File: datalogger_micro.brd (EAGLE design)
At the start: 33 x 38.1 mm, 41 parts, among them IC1 DS3231/SO, IC3 LD117AS33TR, M0 PAT, M1 PAT

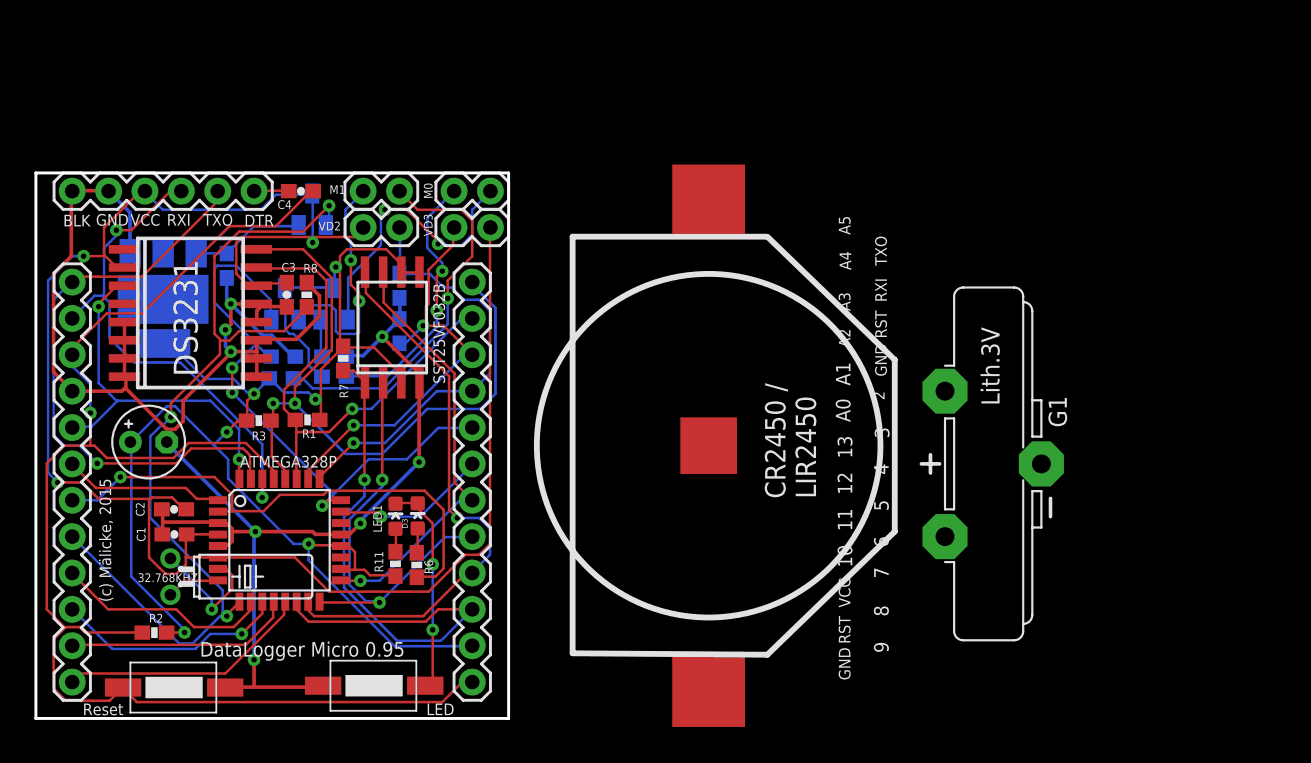
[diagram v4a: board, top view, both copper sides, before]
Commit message: one-sided
moved layout to one sided again, use SMT battery pack.
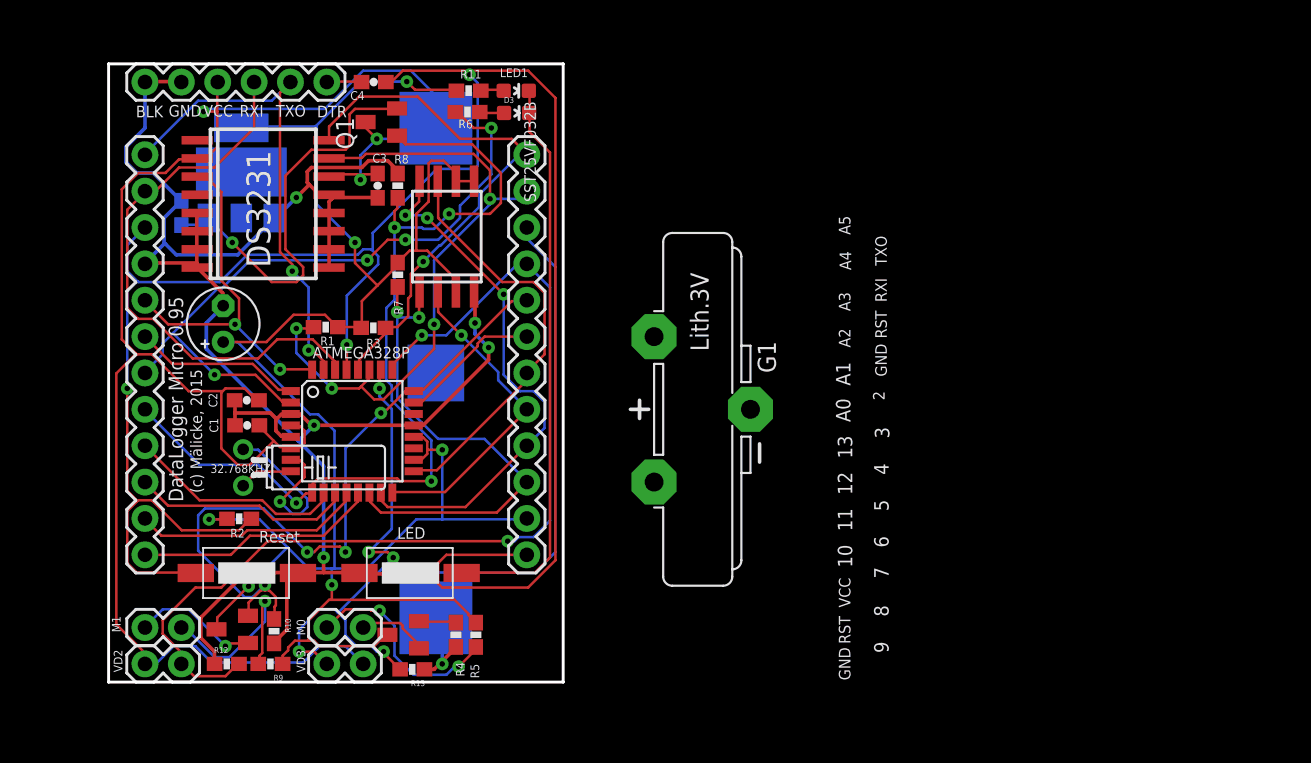
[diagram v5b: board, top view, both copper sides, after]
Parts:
- moved M1 34.1 mm to (7.62, 6.35)
- moved VD2 34.1 mm to (7.62, 3.81)
- moved R11 33.4 mm to (30.2, 43.8), turned to 180 degrees
- moved R6 31.8 mm to (30.1, 42.4), turned to 0 degrees
- moved VD3 31.8 mm to (22.9, 3.81)
- moved M0 31.8 mm to (22.9, 6.35)
- moved LED1 30.9 mm to (33.6, 43.8), turned to 270 degrees
- moved R12 29.0 mm to (13.3, 3.81), flipped to the top, turned to 0 degrees
- moved D3 29.0 mm to (33.6, 42.3), turned to 270 degrees
- moved R13 23.6 mm to (26.3, 3.43), flipped to the top, turned to 180 degrees
- moved Q2 23.6 mm to (25.7, 5.84), flipped to the top, turned to 90 degrees
- moved Q3 23.0 mm to (13.7, 6.22), flipped to the top, turned to 90 degrees
- moved R5 21.2 mm to (29.3, 5.84), flipped to the top, turned to 270 degrees
- moved G1 20.7 mm to (45.7, 21.6)
- moved R4 20.6 mm to (30.7, 5.84), flipped to the top, turned to 270 degrees
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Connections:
- net GND: no longer G1.-
- net VCC/2: no longer G1.+
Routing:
- net RESET: track 100.4 -> 145.8 mm, vias 1 -> 3
- net A3: track 29.6 -> 70.9 mm, vias 2 -> 5
- net A2: track 30.1 -> 69.6 mm, vias 1 -> 2
- net VCC-ST: track 114.1 -> 151.4 mm
- net GNDA: track 15.0 -> 39.9 mm, vias 2 -> 0
- net N$1: track 7.99 -> 29.3 mm, vias 0 -> 1
- net N$6: track 19.8 -> 5.05 mm, vias 2 -> 0
- net N$8: track 26.8 -> 13.8 mm
- net A5: track 48.9 -> 38.1 mm, vias 2 -> 1
- net D4: track 36.6 -> 47.4 mm, vias 1 -> 4
- net GND: track 139.9 -> 149.6 mm, vias 8 -> 7
- net A4: track 36.3 -> 45.7 mm, vias 1 -> 4
- net N$5: track 17.2 -> 8.90 mm, vias 2 -> 1
- net A1: track 42.6 -> 50.5 mm, vias 3 -> 4
- net MISO: track 30.4 -> 22.6 mm, vias 2 -> 1
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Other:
- board size 33 x 38.1 mm -> 31.8 x 43.2 mm

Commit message: schematic adaptions
a lot of schematic adaptions. included various C and Rs were neceassary.
MOSFET instead of Transistor on LM1117..
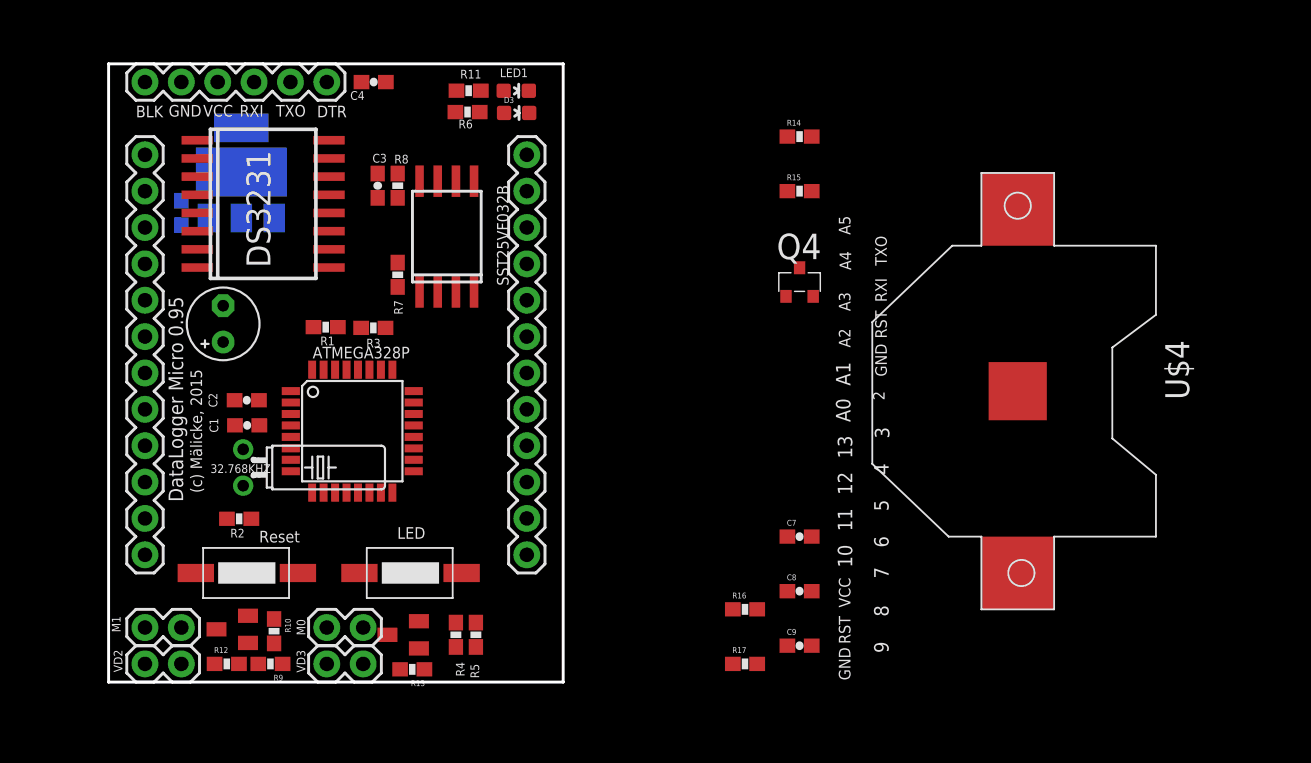
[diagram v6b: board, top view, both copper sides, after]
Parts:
- removed G1: CR2450V, battery:CR2450V
- removed Q1: (no value), semicon-smd-ipc:SOT23
- removed U$3: CR2450SMT, battery:CR2450SMT
- added C7, C8, C9: 0.1uF, SparkFun:0603-CAP
- added Q4: IRLML5203, transistor-power:MICRO3
- added R14, R15, R16, R17: VAR, SparkFun:0603-RES
- added U$4: LIR2032, adafruit:CR2032-SMD
- R8: value 10k -> 100k
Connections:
- net A2: now also R14.1
- net A3: now also R15.1
- net A6: now also ATMEGA328P.19, R16.2, R17.2; no longer IC1.4
- net D2: no longer IC1.3
- net D5: now also Q4.1; no longer Q1.1
- net GND: now also C7.1, C8.1, C9.1, Q4.2, R17.1, U$4.-; no longer IC3.1, U$3.P$2
- net N$1: now also IC3.1, Q4.3; no longer C6.1, IC3.3, Q1.2
- net VCC-ST: now also C9.2; no longer ATMEGA328P.18, R1.2, R3.2
- net VCC/2: now also ATMEGA328P.18, C6.1, C7.2, C8.2, IC3.3, R1.2, R14.2, R15.2, R16.1, R3.2, U$4.+$1, U$4.+$2; no longer Q1.3, U$3.P$3
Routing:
- net VCC-ST: track 151.4 -> 0.00 mm, vias 6 -> 0
- net GND: track 149.6 -> 0.00 mm, vias 7 -> 0
- net RESET: track 145.8 -> 0.00 mm, vias 3 -> 0
- net VCC/2: track 124.2 -> 0.00 mm, vias 3 -> 0
- net A3: track 70.9 -> 0.00 mm, vias 5 -> 0
- net A2: track 69.6 -> 0.00 mm, vias 2 -> 0
- net D5: track 63.9 -> 0.00 mm, vias 4 -> 0
- net A1: track 50.5 -> 0.00 mm, vias 4 -> 0
- net D4: track 47.4 -> 0.00 mm, vias 4 -> 0
- net A4: track 45.7 -> 0.00 mm, vias 4 -> 0
- net GNDA: track 39.9 -> 0.00 mm
- net RXI: track 39.1 -> 0.00 mm
- net A5: track 38.1 -> 0.00 mm, vias 1 -> 0
- net MOSI: track 37.4 -> 0.00 mm, vias 3 -> 0
- net D10: track 35.4 -> 0.00 mm, vias 2 -> 0
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
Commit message: schematics finalized
schematics are finalized and will be verified
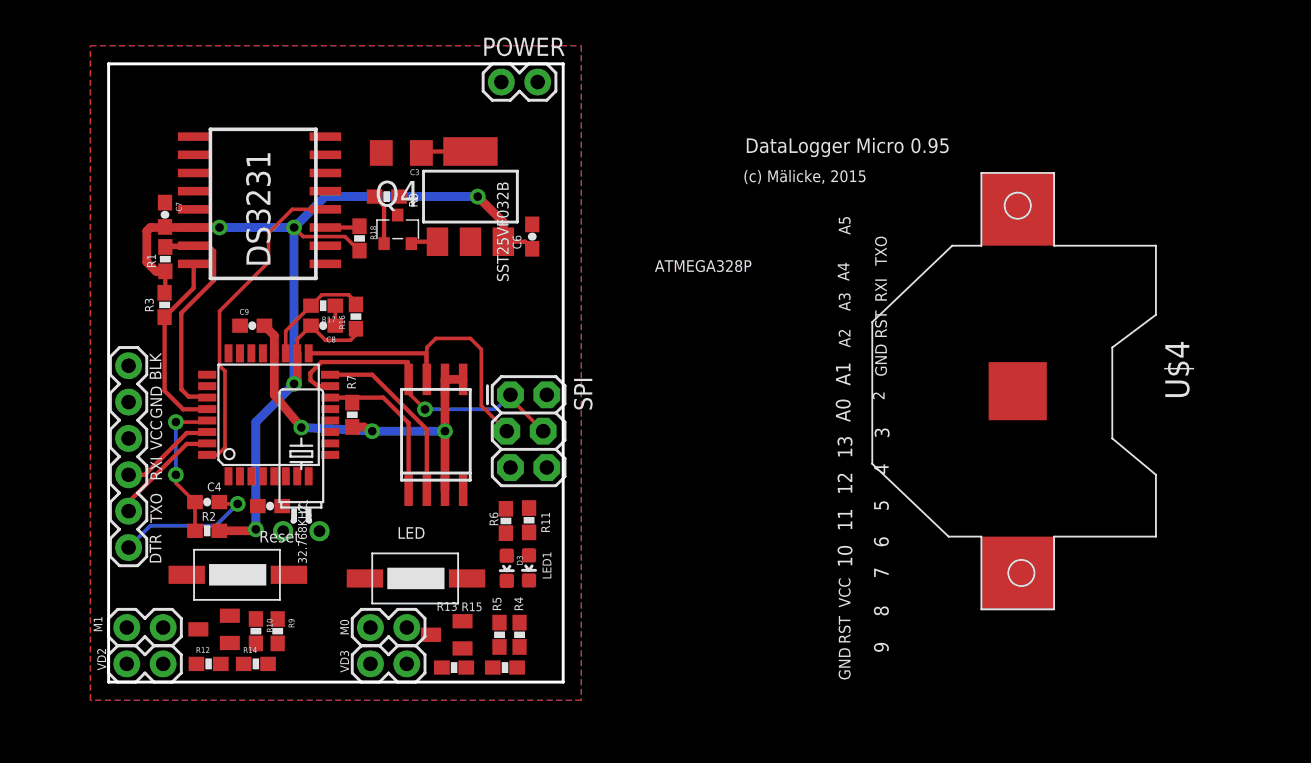
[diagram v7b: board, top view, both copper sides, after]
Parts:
- removed C2: 0.1uF, SparkFun:0603-CAP
- removed C5: 10uF, rcl:E2,5-5
- removed JP3, JP7: (no value), SparkFun:1X12
- added POWER: (no value), SparkFun:1X02
- added R18: 10k, SparkFun:0603-RES
- added SPI: SPI, SparkFun-Connectors:2X3_LOCK
- C3: value 0.1uF -> 10uF; device SparkFun:0603-CAP -> SparkFun:1206
- moved R14 52.9 mm to (15.4, 3.81)
- moved C7 49.7 mm to (9.02, 35.2), turned to 270 degrees
- moved C9 44.3 mm to (15.1, 27.4)
- moved R15 39.1 mm to (32.8, 3.56)
- moved R17 38.7 mm to (20.1, 28.8), turned to 180 degrees
- moved C8 38.1 mm to (20.1, 27.4), turned to 180 degrees
- moved JP1 35.3 mm to (6.48, 11.9), turned to 90 degrees
- moved R16 34.0 mm to (22.4, 28.1), turned to 90 degrees
- moved LED1 33.3 mm to (34.4, 10.5), turned to 180 degrees
- moved D3 31.8 mm to (32.9, 10.5), turned to 180 degrees
- moved C4 31.6 mm to (12.0, 15.1), turned to 0 degrees
- moved R11 30.3 mm to (34.4, 13.8), turned to 90 degrees
- moved R6 28.7 mm to (32.8, 13.8), turned to 270 degrees
- moved Q4 28.3 mm to (25.3, 34.2)
- moved C6 24.6 mm to (34.7, 33.7), flipped to the top
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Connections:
- removed net VCC/2: ATMEGA328P.18, ATMEGA328P.4, ATMEGA328P.6, C1.2, C2.1, C3.2, C6.1, C7.2, C8.2, IC1.14, IC1.2, IC3.3, JP1.4, R1.2, R14.2, R15.2, R16.1, R3.2, U$4.+$1, U$4.+$2, VD2.1, VD3.1
- new net VBAT: ATMEGA328P.18, ATMEGA328P.4, ATMEGA328P.6, C1.2, C6.1, C7.2, C8.2, IC1.14, IC3.3, POWER.2, R1.2, R14.2, R15.2, R16.1, R18.2, R2.2, R3.2, U$4.+$1, U$4.+$2, VD2.1, VD3.1
- net A0: no longer JP3.7
- net A1: no longer JP3.8
- net A2: no longer JP3.9
- net A3: no longer JP3.10
- net A4: no longer JP3.11
- net A5: no longer JP3.12
- net D10: no longer JP3.3
- net D2: now also IC1.4; no longer JP7.8
- net D3: no longer JP7.7
- net D4: no longer JP7.6
- net D5: no longer JP7.5
- net D6: no longer JP7.4
- net D7: now also IC1.2; no longer JP7.3
- net D8: now also IC1.3, R18.1; no longer JP7.2
- net D9: no longer JP7.1
- net GND: now also C3.2, POWER.1, Q4.3, SPI.6; no longer C2.2, C3.1, C5.-, JP7.9, Q4.2
- net MISO: no longer JP3.5
- net MOSI: now also SPI.1, SPI.4; no longer JP3.4
- net N$1: now also Q4.2; no longer Q4.3
- net RESET: now also SPI.5; no longer JP3.1, JP7.10
- net RXI: no longer JP7.11
- net SCK: now also SPI.3; no longer JP3.6
- net TXO: no longer JP7.12
- net VCC-ST: now also C3.1; no longer C5.+, JP3.2, R2.2
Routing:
- net VBAT: track 0.00 -> 74.2 mm, vias 0 -> 5
- net VCC-ST: track 0.00 -> 32.1 mm, vias 0 -> 3
- net SCK: track 0.00 -> 23.1 mm
- net MOSI: track 0.00 -> 22.8 mm, vias 0 -> 1
- net D2: track 0.00 -> 22.7 mm
- net A4: track 0.00 -> 18.2 mm
- net A5: track 0.00 -> 13.2 mm
- net MISO: track 0.00 -> 12.6 mm
- net D10: track 0.00 -> 10.6 mm
- net RESET: track 0.00 -> 10.4 mm, vias 0 -> 2
- net DTR: track 0.00 -> 10.2 mm, vias 0 -> 1
- net A6: track 0.00 -> 7.88 mm
- net TXO: track 0.00 -> 7.82 mm
- net RXI: track 0.00 -> 6.73 mm
- net D5: track 0.00 -> 3.56 mm
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- added copper zone on layer 1, net GND
- added copper zone on layer 16, net GND

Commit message: routing
Routing is 90% complete
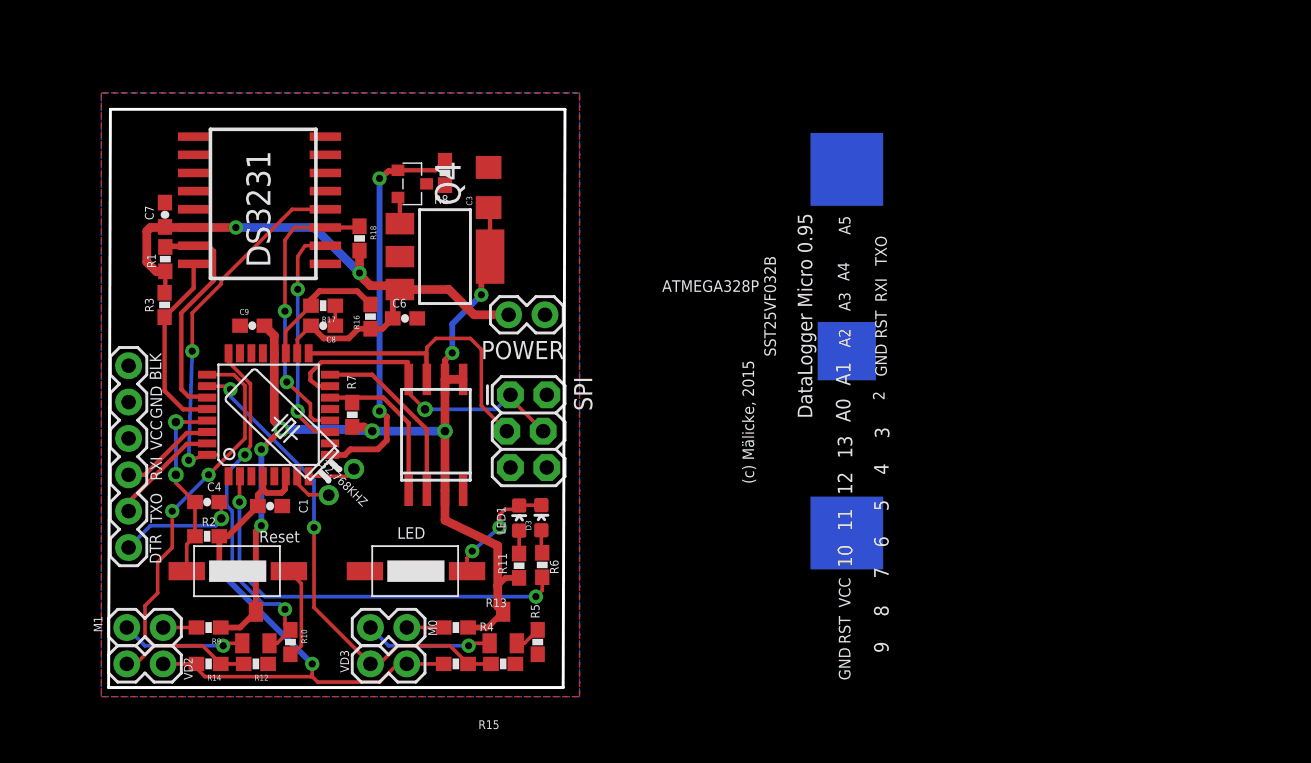
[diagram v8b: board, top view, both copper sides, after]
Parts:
- moved POWER 16.5 mm to (35.6, 28.2), turned to 180 degrees
- moved U$4 12.3 mm to (56.6, 25.7), flipped to the bottom
- moved C6 10.6 mm to (25.8, 27.9), turned to 0 degrees
- moved C3 6.56 mm to (31.6, 37.1), turned to 90 degrees
- moved R9 4.83 mm to (12.1, 6.35), turned to 180 degrees
- moved IC3 4.55 mm to (28.6, 32.3), turned to 270 degrees
- moved R4 4.47 mm to (29.3, 6.35), turned to 180 degrees
- moved 32.768KHZ 4.42 mm to (21.3, 16.5), turned to 46 degrees
- moved R8 4.39 mm to (28.6, 38.1), turned to 270 degrees
- moved D3 4.28 mm to (35.3, 14.0), turned to 0 degrees
- moved R6 3.98 mm to (35.4, 10.7), turned to 90 degrees
- moved Q2 3.97 mm to (32.6, 6.35), turned to 0 degrees
- moved LED1 3.55 mm to (33.8, 14.0), turned to 0 degrees
- moved R13 3.44 mm to (32.6, 3.81)
- moved R15 3.44 mm to (29.3, 3.81), turned to 180 degrees
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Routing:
- net VCC-ST: track 32.1 -> 74.9 mm, vias 3 -> 7
- net A3: track 0.00 -> 34.4 mm, vias 0 -> 2
- net A2: track 0.00 -> 33.5 mm, vias 0 -> 2
- net D4: track 0.00 -> 29.6 mm, vias 0 -> 2
- net A1: track 0.00 -> 24.9 mm, vias 0 -> 2
- net D5: track 3.56 -> 28.0 mm, vias 0 -> 2
- net D8: track 2.42 -> 20.3 mm, vias 0 -> 2
- net D7: track 0.00 -> 16.1 mm, vias 0 -> 2
- net VBAT: track 74.2 -> 88.9 mm, vias 5 -> 4
- net N$6: track 0.00 -> 8.89 mm, vias 0 -> 1
- net N$5: track 0.00 -> 8.66 mm, vias 0 -> 1
- net GNDA: track 0.00 -> 8.13 mm, vias 0 -> 2
- net GND: track 1.40 -> 7.97 mm
- net N$3: track 0.00 -> 3.37 mm
- net RESET: track 10.4 -> 13.4 mm
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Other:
- board size 31.8 x 43.2 mm -> 31.9 x 40.4 mm
